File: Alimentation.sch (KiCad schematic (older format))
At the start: 21 parts, among them P1 Prise_Equilibrage, P10 CONN_01X02, P2 Prise_Alim, P3 Prise_Batterie, P4 ConnecteurBippeur, P5 CONN_01X04, P6 CAN_conn, P7 CAN_conn, P8 CONN_01X02, P9 CONN_01X02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

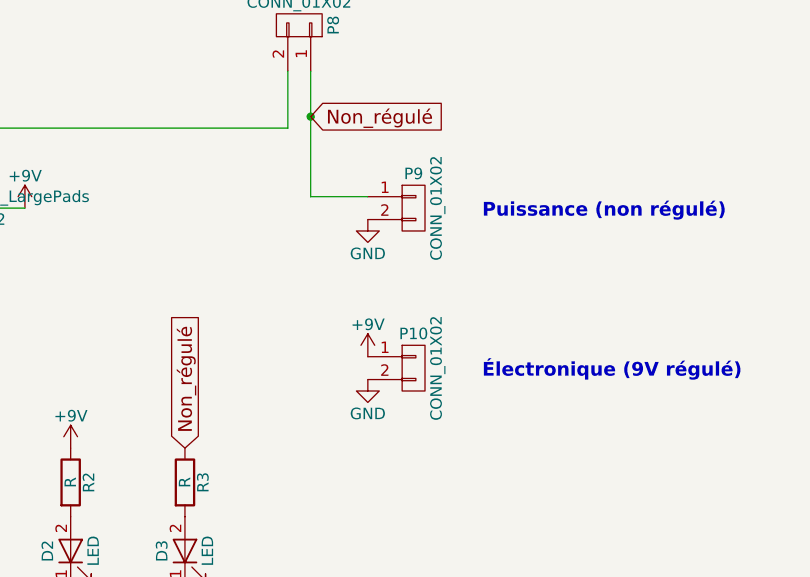
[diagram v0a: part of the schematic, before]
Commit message: pin 1 des connecteurs sur la masse
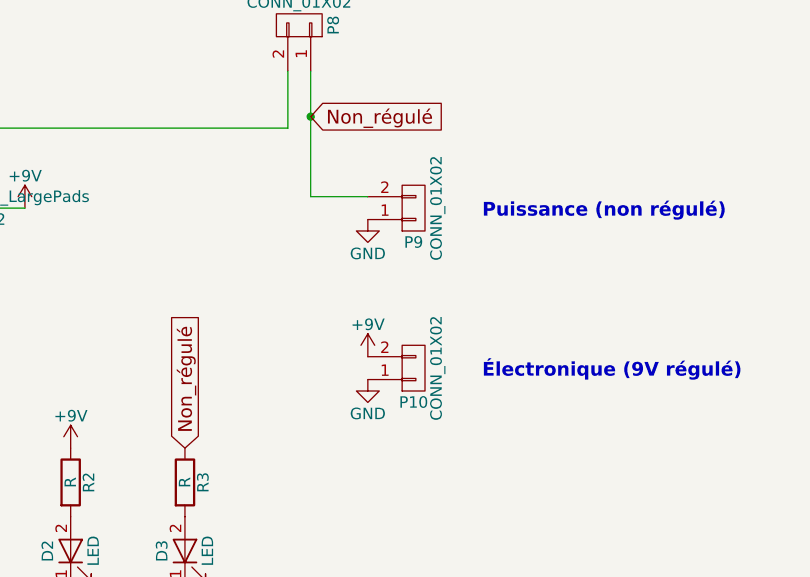
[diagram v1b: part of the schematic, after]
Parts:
- P10, P2, P3, P9: footprint Connectors_Phoenix:PhoenixContact_MSTBVA-G_02x5.00mm_Vertical -> Connectors_Phoenix:PhoenixContact_MC-G_02x3.50mm_Angled
- P5: footprint Terminal_Blocks:TerminalBlock_Pheonix_MPT-2.54mm_4pol -> Connectors_Phoenix:PhoenixContact_MC-G_04x3.50mm_Angled
- P8: footprint Terminal_Blocks:TerminalBlock_Pheonix_MPT-2.54mm_2pol -> Connectors_Phoenix:PhoenixContact_MC-G_02x3.50mm_Angled
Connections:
- net +9V: now also P10.2 (P2); no longer P10.1 (P1)
- net GND: now also P10.1 (P1), P9.1 (P1); no longer P10.2 (P2), P9.2 (P2)
- net Non_régulé: now also P9.2 (P2); no longer P9.1 (P1)
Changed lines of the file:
@@
 F 0 "P3" H 1700 3900 50  0000 C CNN
 F 1 "Prise_Batterie" V 1800 3750 50  0000 C CNB
-F 2 "Connectors_Phoenix:PhoenixContact_MSTBVA-G_02x5.00mm_Vertical" H 1700 3750 50  0001 C CNN
+F 2 "Connectors_Phoenix:PhoenixContact_MC-G_02x3.50mm_Angled" H 1700 3750 50  0001 C CNN
 F 3 "" H 1700 3750 50  0000 C CNN
 	1    1700 3750
@@
 F 0 "P9" H 9100 3250 50  0000 C CNN
 F 1 "CONN_01X02" V 9200 3100 50  0000 C CNN
-F 2 "Connectors_Phoenix:PhoenixContact_MSTBVA-G_02x5.00mm_Vertical" H 9100 3100 50  0001 C CNN
+F 2 "Connectors_Phoenix:PhoenixContact_MC-G_02x3.50mm_Angled" H 9100 3100 50  0001 C CNN
 F 3 "" H 9100 3100 50  0000 C CNN
 	1    9100 3100
-	1    0    0    -1
+	1    0    0    1
 $EndComp
 $Comp
@@
 F 0 "P10" H 9100 3950 50  0000 C CNN
 F 1 "CONN_01X02" V 9200 3800 50  0000 C CNN
-F 2 "Connectors_Phoenix:PhoenixContact_MSTBVA-G_02x5.00mm_Vertical" H 9100 3800 50  0001 C CNN
+F 2 "Connectors_Phoenix:PhoenixContact_MC-G_02x3.50mm_Angled" H 9100 3800 50  0001 C CNN
 F 3 "" H 9100 3800 50  0000 C CNN
 	1    9100 3800
-	1    0    0    -1
+	1    0    0    1
 $EndComp
 Text Notes 9400 3150 0    60   ~ 12
@@
 F 0 "P2" H 1700 2950 50  0000 C CNN
 F 1 "Prise_Alim" V 1800 2800 50  0000 C CNB
-F 2 "Connectors_Phoenix:PhoenixContact_MSTBVA-G_02x5.00mm_Vertical" H 1700 2800 50  0001 C CNN
+F 2 "Connectors_Phoenix:PhoenixContact_MC-G_02x3.50mm_Angled" H 1700 2800 50  0001 C CNN
 F 3 "" H 1700 2800 50  0000 C CNN
 	1    1700 2800
@@
 F 0 "P8" H 8600 2450 50  0000 C CNN
 F 1 "CONN_01X02" V 8700 2300 50  0000 C CNN
-F 2 "Terminal_Blocks:TerminalBlock_Pheonix_MPT-2.54mm_2pol" H 8600 2300 50  0001 C CNN
+F 2 "Connectors_Phoenix:PhoenixContact_MC-G_02x3.50mm_Angled" H 8600 2300 50  0001 C CNN
 F 3 "" H 8600 2300 50  0000 C CNN
 	1    8600 2300
@@
 F 0 "P5" H 3400 2550 50  0000 C CNN
 F 1 "CONN_01X04" V 3500 2300 50  0000 C CNN
-F 2 "Terminal_Blocks:TerminalBlock_Pheonix_MPT-2.54mm_4pol" H 3400 2300 50  0001 C CNN
+F 2 "Connectors_Phoenix:PhoenixContact_MC-G_04x3.50mm_Angled" H 3400 2300 50  0001 C CNN
 F 3 "" H 3400 2300 50  0000 C CNN
 	1    3400 2300

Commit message: clean+fix cache libs + new lib path
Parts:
- D2, D3: symbol LED-RESCUE-Alimentation -> LED
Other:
- moved on the sheet: RV1
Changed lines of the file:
@@
 EESchema Schematic File Version 2
-LIBS:Alimentation-rescue
+LIBS:74xx
+LIBS:adc-dac
+LIBS:analog_switches
+LIBS:atmel
+LIBS:audio
+LIBS:cmos4000
+LIBS:conn
+LIBS:contrib
+LIBS:cypress
+LIBS:device
+LIBS:digital-audio
+LIBS:display
+LIBS:dsp
+LIBS:intel
+LIBS:interface
+LIBS:linear
+LIBS:memory
+LIBS:microchip
+LIBS:microcontrollers
+LIBS:motorola
+LIBS:opto
+LIBS:philips
 LIBS:power
-LIBS:device
+LIBS:regul
+LIBS:siliconi
+LIBS:texas
 LIBS:transistors
-LIBS:conn
-LIBS:linear
-LIBS:regul
-LIBS:74xx
-LIBS:cmos4000
-LIBS:adc-dac
-LIBS:memory
+LIBS:valves
 LIBS:xilinx
-LIBS:microcontrollers
-LIBS:dsp
-LIBS:microchip
-LIBS:analog_switches
-LIBS:motorola
-LIBS:texas
-LIBS:intel
-LIBS:audio
-LIBS:interface
-LIBS:digital-audio
-LIBS:philips
-LIBS:display
-LIBS:cypress
-LIBS:siliconi
-LIBS:opto
-LIBS:atmel
-LIBS:contrib
-LIBS:valves
 LIBS:Infineon
 LIBS:Microchip
+LIBS:Panchip
 LIBS:PhoenixRobotik
 LIBS:STMicroelectronics
-LIBS:Alimentation-cache
 EELAYER 25 0
 EELAYER END
@@
 encoding utf-8
 Sheet 1 1
-Title ""
-Date ""
+Title "Carte Alimentation 2017"
+Date "2017-02"
 Rev ""
-Comp ""
+Comp "Phoenix Robotik"
 Comment1 ""
 Comment2 ""
@@
 F 0 "U1" H 6550 3400 50  0000 C CNN
 F 1 "LD1084V" H 6550 3350 50  0000 C CNN
-F 2 "TO_SOT_Packages_THT:TO-220_Neutral123_Horizontal_LargePads" H 6550 3250 50  0000 C CNN
+F 2 "TO_SOT_Packages_THT:TO-220_Neutral123_Horizontal_LargePads" H 6550 3250 50  0001 C CNN
 F 3 "" H 6550 3150 50  0000 C CNN
 	1    6550 3150
@@
 $EndComp
 $Comp
-L LED-RESCUE-Alimentation D2
+L LED D2
 U 1 1 5885E455
 P 7600 4600
@@
 $EndComp
 $Comp
-L LED-RESCUE-Alimentation D3
+L LED D3
 U 1 1 5885F579
 P 8100 4600
@@
 F 3 "" H 4150 3100 50  0000 C CNN
 	1    4150 3100
-	1    0    0    -1
+	-1   0    0    1
 $EndComp
 Wire Wire Line
@@
 F 3 "" H 6550 3650 50  0000 C CNN
 	1    6550 3650
-	0    1    1    0
-$EndComp
-$Comp
+	1    0    0    -1
+$EndComp
+$Comp
